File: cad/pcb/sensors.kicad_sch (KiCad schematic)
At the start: 9 parts

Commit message: add power section on pcb layout
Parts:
- renumbered C19 to C20, TP12 to TP11
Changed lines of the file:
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@@
   (symbol (lib_id "power:+3.3V") (at 82.55 45.72 0) (unit 1)
     (in_bom yes) (on_board yes)
-    (property "Reference" "#PWR073" (id 0) (at 82.55 49.53 0)
+    (property "Reference" "#PWR075" (id 0) (at 82.55 49.53 0)
       (effects (font (size 1.27 1.27)) hide)
     )
@@
   (symbol (lib_id "power:GND") (at 49.53 67.31 0) (unit 1)
     (in_bom yes) (on_board yes)
-    (property "Reference" "#PWR077" (id 0) (at 49.53 73.66 0)
+    (property "Reference" "#PWR079" (id 0) (at 49.53 73.66 0)
       (effects (font (size 1.27 1.27)) hide)
     )
@@
   (symbol (lib_id "power:+3.3V") (at 170.18 63.5 0) (unit 1)
     (in_bom yes) (on_board yes)
-    (property "Reference" "#PWR076" (id 0) (at 170.18 67.31 0)
+    (property "Reference" "#PWR078" (id 0) (at 170.18 67.31 0)
       (effects (font (size 1.27 1.27)) hide)
     )
@@
   (symbol (lib_id "power:GND") (at 87.63 143.51 0) (unit 1)
     (in_bom yes) (on_board yes)
-    (property "Reference" "#PWR082" (id 0) (at 87.63 149.86 0)
+    (property "Reference" "#PWR084" (id 0) (at 87.63 149.86 0)
       (effects (font (size 1.27 1.27)) hide)
     )
@@
   (symbol (lib_id "power:GND") (at 176.53 53.34 0) (unit 1)
     (in_bom yes) (on_board yes)
-    (property "Reference" "#PWR075" (id 0) (at 176.53 59.69 0)
+    (property "Reference" "#PWR077" (id 0) (at 176.53 59.69 0)
       (effects (font (size 1.27 1.27)) hide)
     )
@@
   (symbol (lib_id "power:GND") (at 82.55 67.31 0) (unit 1)
     (in_bom yes) (on_board yes)
-    (property "Reference" "#PWR078" (id 0) (at 82.55 73.66 0)
+    (property "Reference" "#PWR080" (id 0) (at 82.55 73.66 0)
       (effects (font (size 1.27 1.27)) hide)
     )
@@
   (symbol (lib_id "power:GND") (at 168.91 96.52 0) (unit 1)
     (in_bom yes) (on_board yes)
-    (property "Reference" "#PWR079" (id 0) (at 168.91 102.87 0)
+    (property "Reference" "#PWR081" (id 0) (at 168.91 102.87 0)
       (effects (font (size 1.27 1.27)) hide)
     )
@@
   (symbol (lib_id "Device:C_Small") (at 82.55 62.23 0) (unit 1)
     (in_bom yes) (on_board yes)
-    (property "Reference" "C19" (id 0) (at 76.2 62.23 0)
+    (property "Reference" "C20" (id 0) (at 76.2 62.23 0)
       (effects (font (size 1.27 1.27)) (justify left))
     )
@@
   (symbol (lib_id "power:GND") (at 222.25 96.52 0) (unit 1)
     (in_bom yes) (on_board yes)
-    (property "Reference" "#PWR080" (id 0) (at 222.25 102.87 0)
+    (property "Reference" "#PWR082" (id 0) (at 222.25 102.87 0)
       (effects (font (size 1.27 1.27)) hide)
     )
@@
   (symbol (lib_id "Connector:TestPoint") (at 104.14 119.38 0) (unit 1)
     (in_bom yes) (on_board yes)
-    (property "Reference" "TP12" (id 0) (at 96.52 115.57 0)
+    (property "Reference" "TP11" (id 0) (at 96.52 115.57 0)
       (effects (font (size 1.27 1.27)) (justify left))
     )
@@
   (symbol (lib_id "power:+3.3V") (at 93.98 45.72 0) (unit 1)
     (in_bom yes) (on_board yes)
-    (property "Reference" "#PWR074" (id 0) (at 93.98 49.53 0)
+    (property "Reference" "#PWR076" (id 0) (at 93.98 49.53 0)
       (effects (font (size 1.27 1.27)) hide)
     )
@@
   (symbol (lib_id "power:+3.3V") (at 87.63 111.76 0) (unit 1)
     (in_bom yes) (on_board yes)
-    (property "Reference" "#PWR081" (id 0) (at 87.63 115.57 0)
-      (effects (font (size 1.27 1.27)) hide)
-    )
+    (property "Reference" "#PWR083" (id 0) (at 87.63 115.57 0)
+      (effects (font (size 1.27 1.27)) hide)
+    )

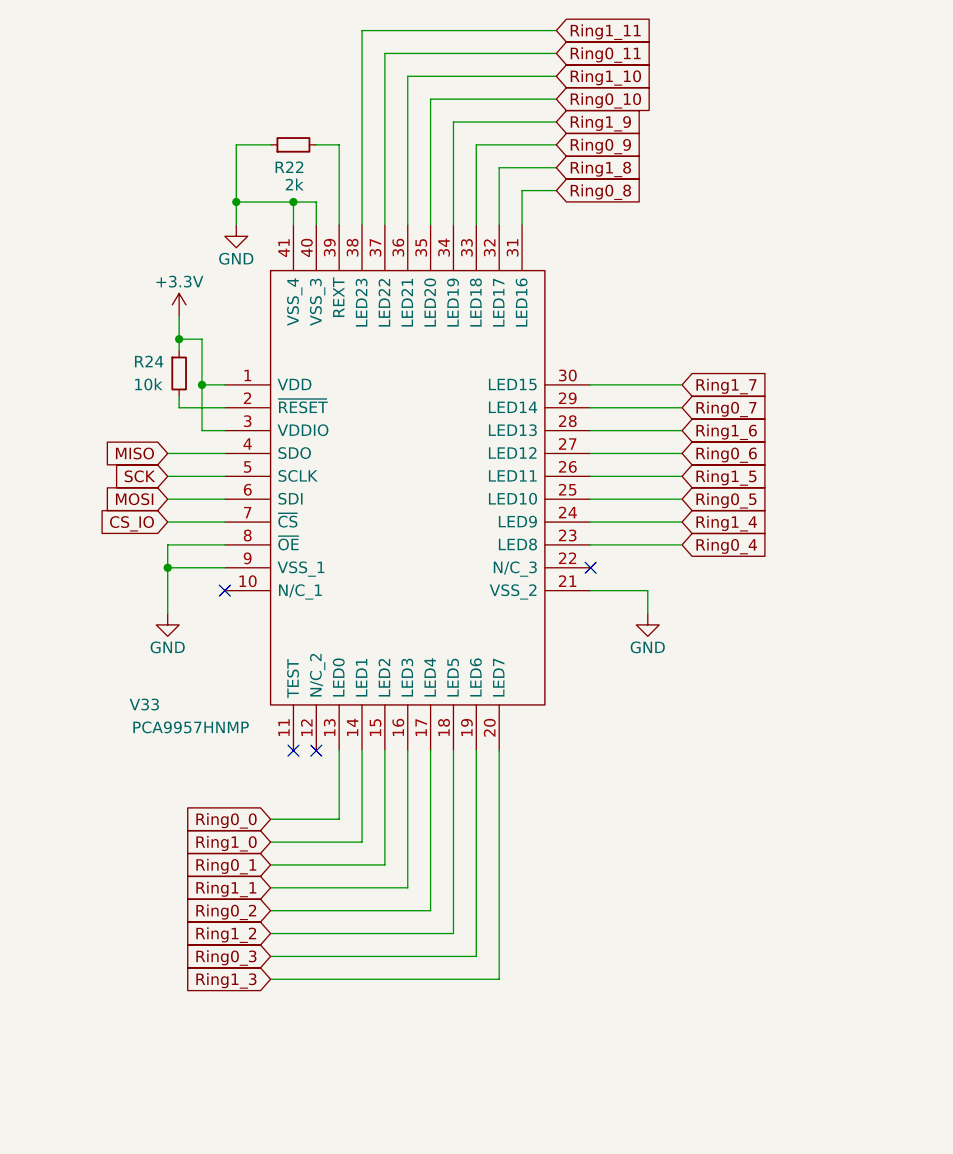
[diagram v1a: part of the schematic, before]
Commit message: add 3d models for pcb layout
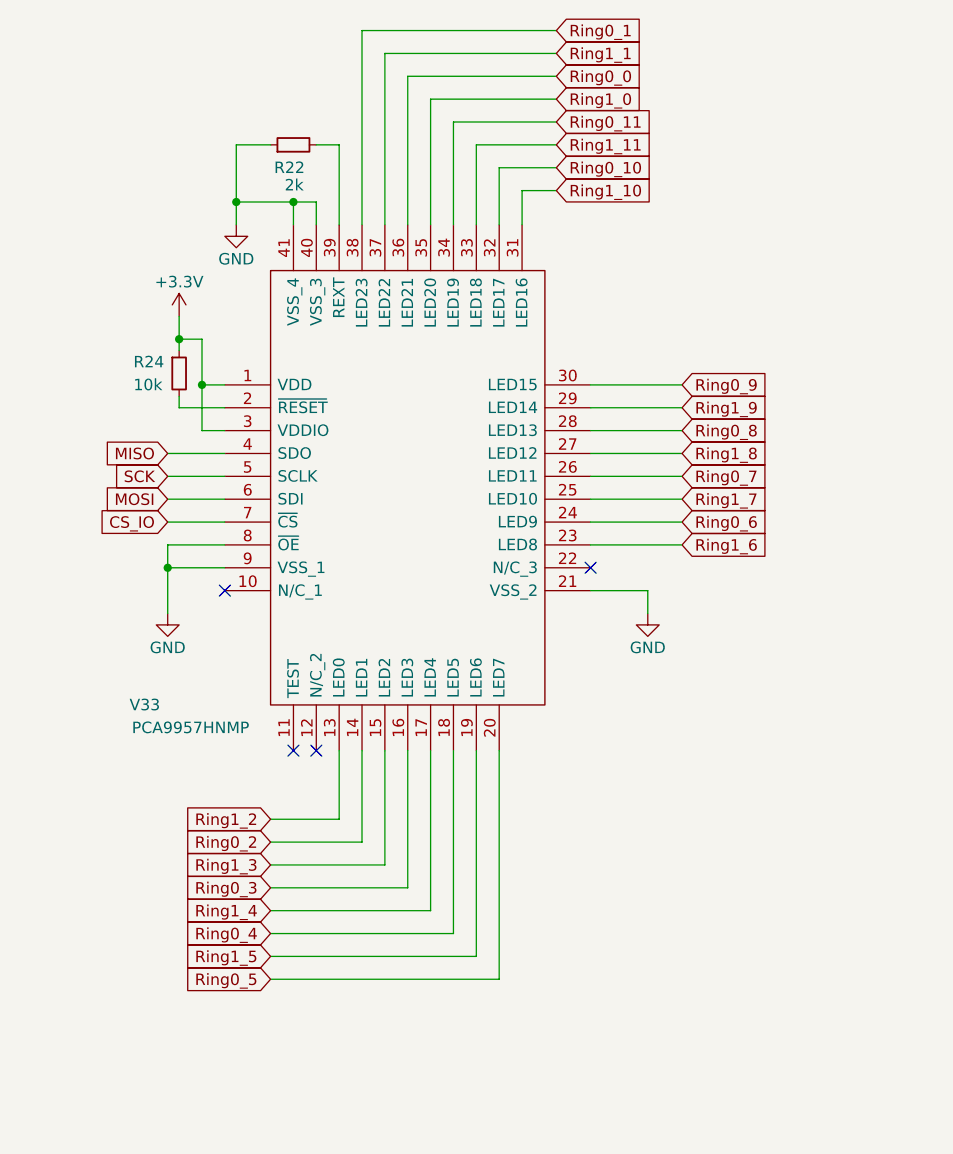
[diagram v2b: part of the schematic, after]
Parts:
- V33: footprint IO Expander:PCA9957HNMP -> Package_DFN_QFN:HVQFN-40-1EP_6x6mm_P0.5mm_EP4.1x4.1mm
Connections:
- net Ring0_0: now also V33.36 (LED21); no longer V33.13 (LED0)
- net Ring0_1: now also V33.38 (LED23); no longer V33.15 (LED2)
- net Ring0_10: now also V33.32 (LED17); no longer V33.35 (LED20)
- net Ring0_11: now also V33.34 (LED19); no longer V33.37 (LED22)
- net Ring0_2: now also V33.14 (LED1); no longer V33.17 (LED4)
- net Ring0_3: now also V33.16 (LED3); no longer V33.19 (LED6)
- net Ring0_4: now also V33.18 (LED5); no longer V33.23 (LED8)
- net Ring0_5: now also V33.20 (LED7); no longer V33.25 (LED10)
- net Ring0_6: now also V33.24 (LED9); no longer V33.27 (LED12)
- net Ring0_7: now also V33.26 (LED11); no longer V33.29 (LED14)
- net Ring0_8: now also V33.28 (LED13); no longer V33.31 (LED16)
- net Ring0_9: now also V33.30 (LED15); no longer V33.33 (LED18)
- net Ring1_0: now also V33.35 (LED20); no longer V33.14 (LED1)
- net Ring1_1: now also V33.37 (LED22); no longer V33.16 (LED3)
- net Ring1_10: now also V33.31 (LED16); no longer V33.36 (LED21)
- net Ring1_11: now also V33.33 (LED18); no longer V33.38 (LED23)
- net Ring1_2: now also V33.13 (LED0); no longer V33.18 (LED5)
- net Ring1_3: now also V33.15 (LED2); no longer V33.20 (LED7)
- net Ring1_4: now also V33.17 (LED4); no longer V33.24 (LED9)
- net Ring1_5: now also V33.19 (LED6); no longer V33.26 (LED11)
- net Ring1_6: now also V33.23 (LED8); no longer V33.28 (LED13)
- net Ring1_7: now also V33.25 (LED10); no longer V33.30 (LED15)
- net Ring1_8: now also V33.27 (LED12); no longer V33.32 (LED17)
- net Ring1_9: now also V33.29 (LED14); no longer V33.34 (LED19)
